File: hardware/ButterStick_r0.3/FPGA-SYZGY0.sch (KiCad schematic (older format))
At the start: 1 part, among them U2 ECP5UM5G_85_CABGA381

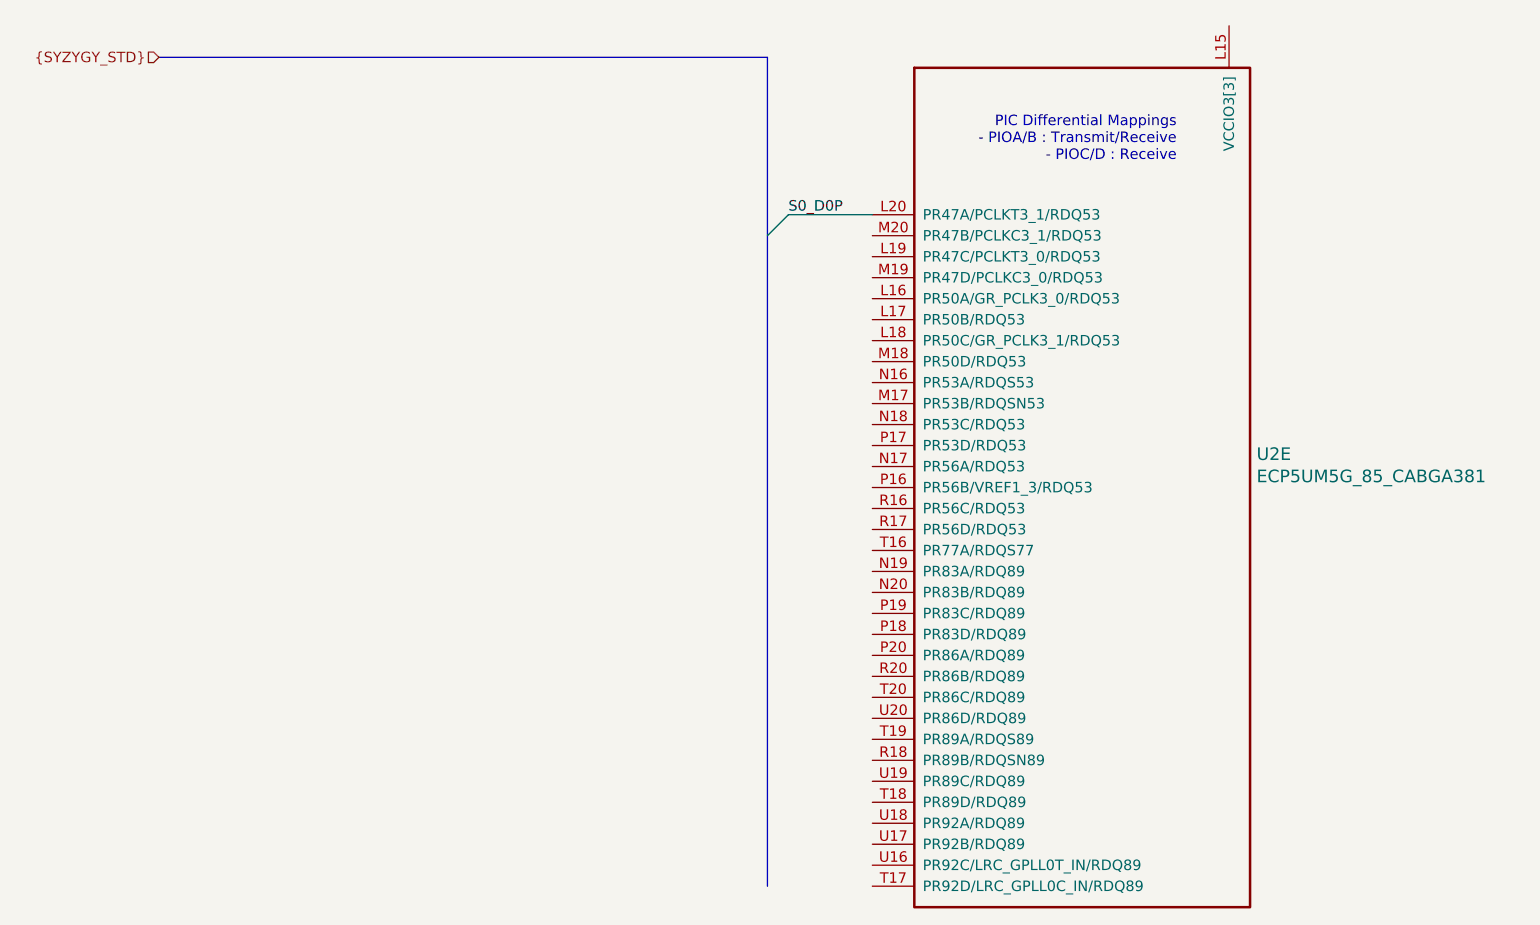
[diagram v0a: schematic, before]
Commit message: hw.r0_3: Start pin assignments for DDR3
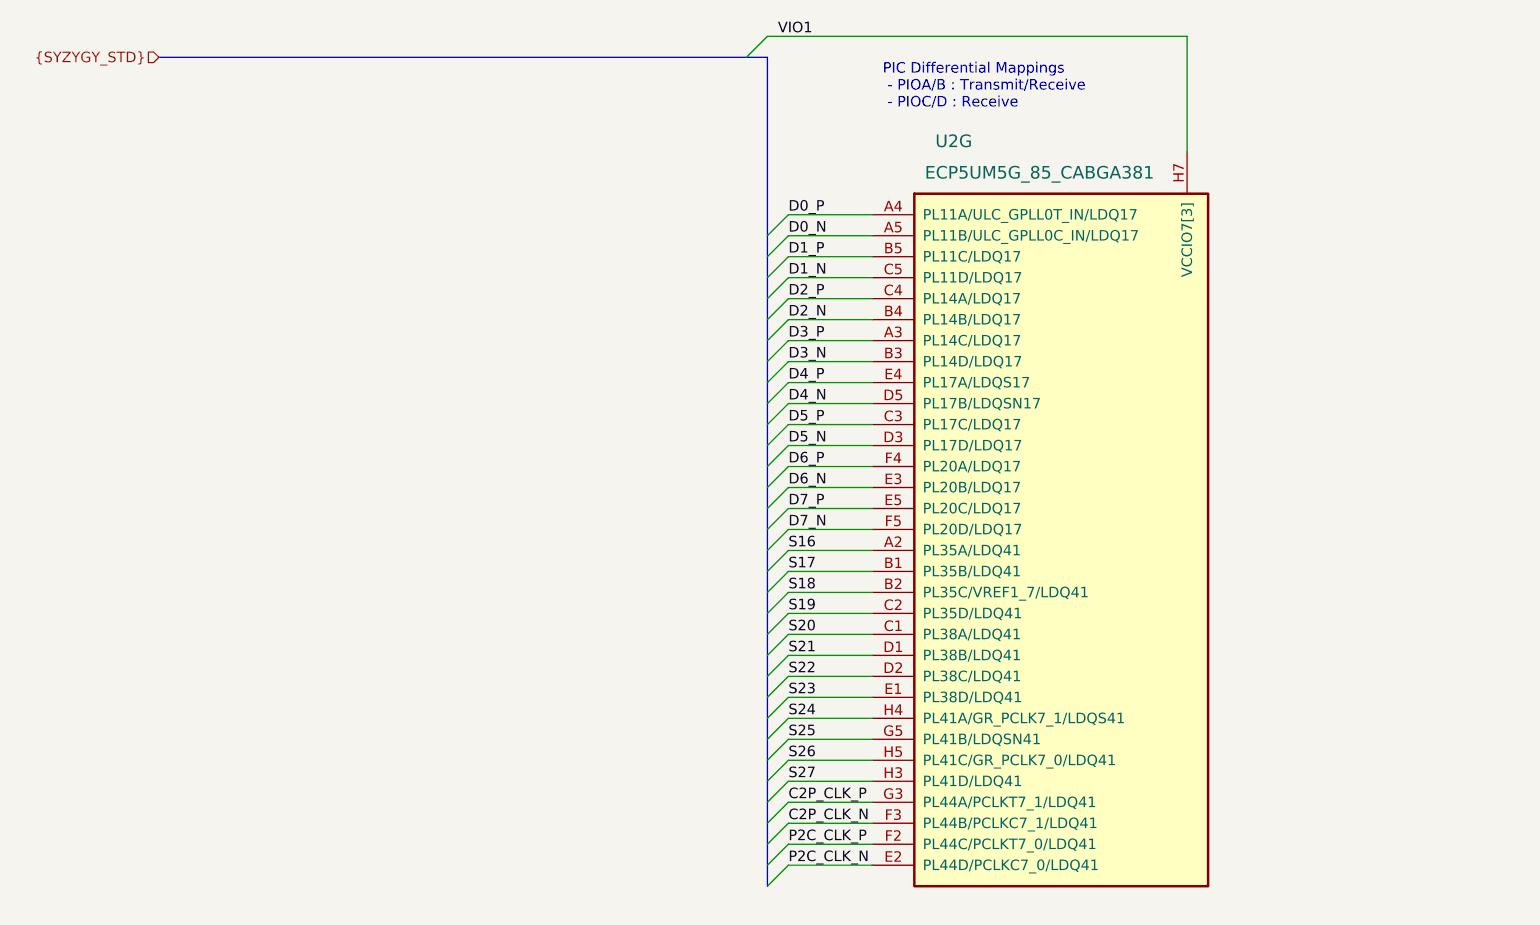
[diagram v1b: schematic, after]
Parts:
- removed U2: ECP5UM5G_85_CABGA381, gkl_housings_bga:caBGA_381_17x17, symbol ECP5UM5G-85Pinout:ECP5UM5G_85_CABGA381
- added U2: ECP5UM5G_85_CABGA381, gkl_housings_bga:caBGA_381_17x17, symbol gkl_lattice:ECP5UM5G_85_CABGA381
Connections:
- new net C2P_CLK_N: U2.F3 (PL44B/PCLKC7_1/LDQ41)
- new net C2P_CLK_P: U2.G3 (PL44A/PCLKT7_1/LDQ41)
- new net D0_N: U2.A5 (PL11B/ULC_GPLL0C_IN/LDQ17)
- new net D0_P: U2.A4 (PL11A/ULC_GPLL0T_IN/LDQ17)
- new net D1_N: U2.C5 (PL11D/LDQ17)
- new net D1_P: U2.B5 (PL11C/LDQ17)
- new net D2_N: U2.B4 (PL14B/LDQ17)
- new net D2_P: U2.C4 (PL14A/LDQ17)
- new net D3_N: U2.B3 (PL14D/LDQ17)
- new net D3_P: U2.A3 (PL14C/LDQ17)
- new net D4_N: U2.D5 (PL17B/LDQSN17)
- new net D4_P: U2.E4 (PL17A/LDQS17)
- new net D5_N: U2.D3 (PL17D/LDQ17)
- new net D5_P: U2.C3 (PL17C/LDQ17)
- new net D6_N: U2.E3 (PL20B/LDQ17)
- new net D6_P: U2.F4 (PL20A/LDQ17)
- new net D7_N: U2.F5 (PL20D/LDQ17)
- new net D7_P: U2.E5 (PL20C/LDQ17)
- new net P2C_CLK_N: U2.E2 (PL44D/PCLKC7_0/LDQ41)
- new net P2C_CLK_P: U2.F2 (PL44C/PCLKT7_0/LDQ41)
- new net S16: U2.A2 (PL35A/LDQ41)
- new net S17: U2.B1 (PL35B/LDQ41)
- new net S18: U2.B2 (PL35C/VREF1_7/LDQ41)
- new net S19: U2.C2 (PL35D/LDQ41)
- new net S20: U2.C1 (PL38A/LDQ41)
- new net S21: U2.D1 (PL38B/LDQ41)
- new net S22: U2.D2 (PL38C/LDQ41)
- new net S23: U2.E1 (PL38D/LDQ41)
- new net S24: U2.H4 (PL41A/GR_PCLK7_1/LDQS41)
- new net S25: U2.G5 (PL41B/LDQSN41)
- new net S26: U2.H5 (PL41C/GR_PCLK7_0/LDQ41)
- new net S27: U2.H3 (PL41D/LDQ41)
- new net VIO1: U2.H6 (VCCIO7[3]), U2.H7 (VCCIO7[3]), U2.J6 (VCCIO7[3])
